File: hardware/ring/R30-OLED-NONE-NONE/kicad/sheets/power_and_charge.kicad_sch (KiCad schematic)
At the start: 19 parts, among them Q1 SI2301 P-FET, Q2 2N7002 gate driver, U3 TP4054, U4 RT9080-33GJ5

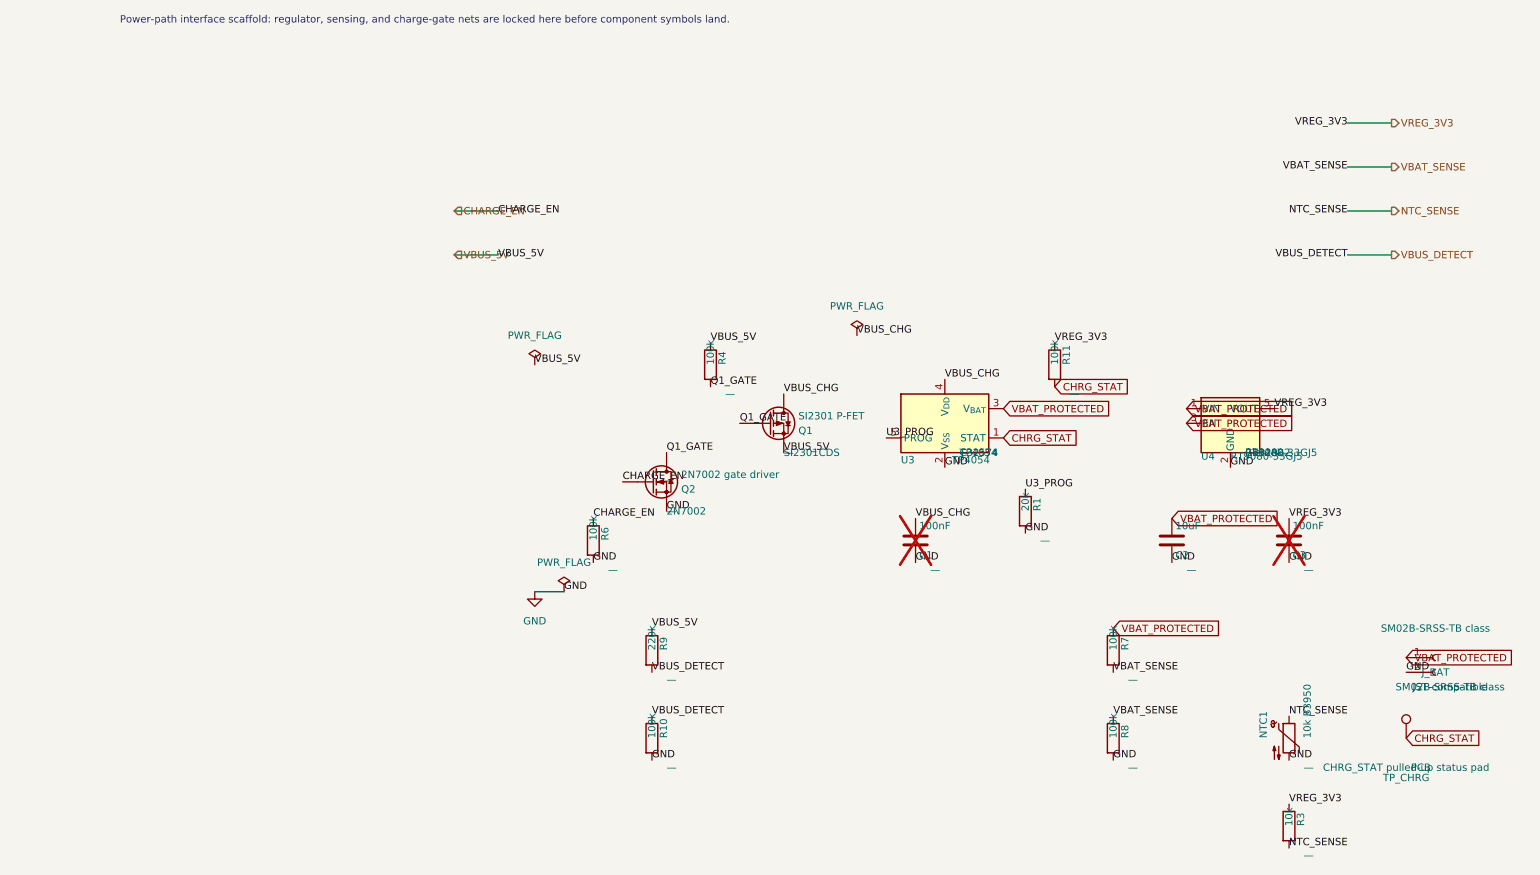
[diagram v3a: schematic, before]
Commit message: fix(r30): reconcile schematic net parity
Sensing mechanism: PAW3204 optical surface tracking.

Form factor and angle: R30 30-degree ring, OLED/NONE/NONE active lane.

Intended use: accessibility-first BLE HID pointing first-board validation.

BOM estimate: active R30 prototype remains about .30-.45, target about .
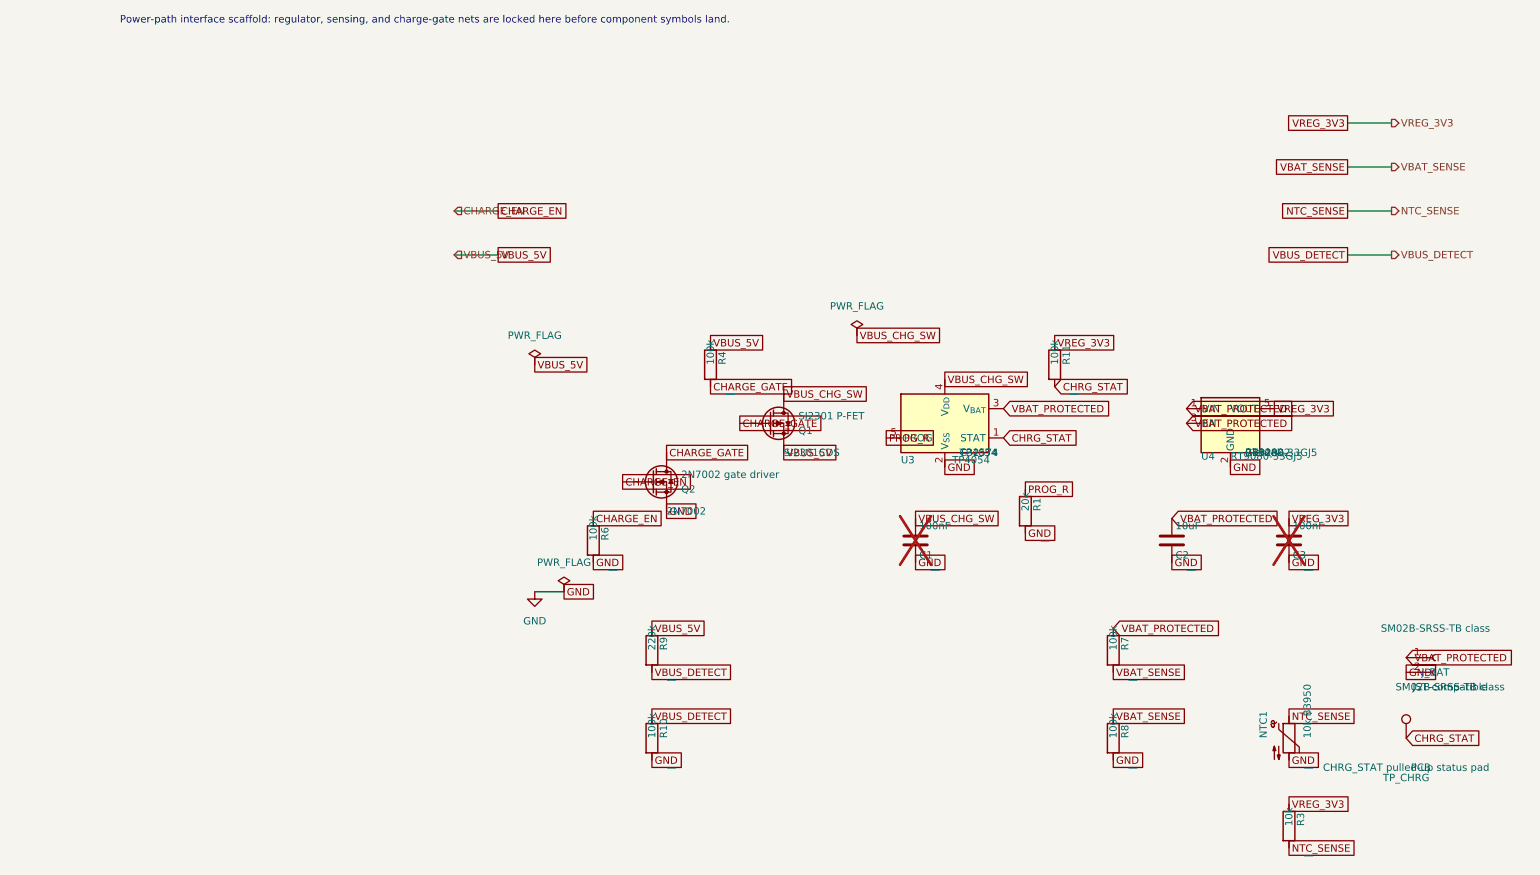
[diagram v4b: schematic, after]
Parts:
- Q1: symbol Device:Q_PMOS -> PowerFinger:SI2301_SOT23_FirstBoard
- Q2: symbol Device:Q_NMOS -> PowerFinger:2N7002_SOT23_FirstBoard
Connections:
- net CHARGE_EN: now also Q2.1 (G); no longer Q2.G
- net GND: now also Q2.2 (S); no longer Q2.S
- net VBUS_5V: now also Q1.3 (S); no longer Q1.S
- removed net Q1_GATE: Q1.G, Q2.D, R4.2
- net U3_PROG renamed PROG_R
- net VBUS_CHG renamed VBUS_CHG_SW
- net VBUS_CHG_SW: now also Q1.2 (D); no longer Q1.D
- new net CHARGE_GATE: Q1.1 (G), Q2.3 (D), R4.2
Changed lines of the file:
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@@
 	(paper "A4")
 	(symbol
-		(lib_id "Device:Q_PMOS")
+		(lib_id "PowerFinger:SI2301_SOT23_FirstBoard")
 		(at 80.01 90.17 0)
 		(unit 1)
@@
 			)
 		)
-		(pin "D"
-		)
-		(pin "G"
-		)
-		(pin "S"
+		(pin "2"
+		)
+		(pin "1"
+		)
+		(pin "3"
 		)
 		(instances
@@
 	)
 	(symbol
-		(lib_id "Device:Q_NMOS")
+		(lib_id "PowerFinger:2N7002_SOT23_FirstBoard")
 		(at 59.69 100.33 0)
 		(unit 1)
@@
 			)
 		)
-		(pin "D"
-		)
-		(pin "G"
-		)
-		(pin "S"
+		(pin "3"
+		)
+		(pin "1"
+		)
+		(pin "2"
 		)
 		(instances
@@
 		)
 	)
-	(label "VBUS_5V"
+	(global_label "VBUS_5V"
+		(shape passive)
 		(at 82.55 95.25 0.0000)
 		(effects
@@
 		)
 	)
-	(label "VBUS_CHG"
+	(global_label "VBUS_CHG_SW"
+		(shape passive)
 		(at 82.55 85.09 0.0000)
 		(effects
@@
 		)
 	)
-	(label "Q1_GATE"
+	(global_label "CHARGE_GATE"
+		(shape passive)
 		(at 74.93 90.17 0.0000)
 		(effects
@@
 		)
 	)
-	(label "Q1_GATE"
+	(global_label "CHARGE_GATE"
+		(shape passive)
 		(at 62.23 95.25 0.0000)
 		(effects
@@
 		)
 	)
-	(label "GND"
+	(global_label "GND"
+		(shape passive)
 		(at 62.23 105.41 0.0000)
 		(effects
@@
 		)
 	)
-	(label "CHARGE_EN"
+	(global_label "CHARGE_EN"
+		(shape passive)
 		(at 54.61 100.33 0.0000)
 		(effects
@@
 		)
 	)
-	(label "VBUS_5V"
+	(global_label "VBUS_5V"
+		(shape passive)
 		(at 69.85 76.2 0.0000)
 		(effects
@@
 		)
 	)
-	(label "Q1_GATE"
+	(global_label "CHARGE_GATE"
+		(shape passive)
 		(at 69.85 83.82 0.0000)
 		(effects
@@
 		)
 	)
-	(label "CHARGE_EN"
+	(global_label "CHARGE_EN"
+		(shape passive)
 		(at 49.53 106.68 0.0000)
 		(effects
@@
 		)
 	)
-	(label "GND"
+	(global_label "GND"
+		(shape passive)
 		(at 49.53 114.3 0.0000)
 		(effects
@@
 		)
 	)
-	(label "GND"
+	(global_label "GND"
+		(shape passive)
 		(at 110.49 97.79 0.0000)
 		(effects
@@
 		)
 	)
-	(label "VBUS_CHG"
+	(global_label "VBUS_CHG_SW"
+		(shape passive)
 		(at 110.49 82.55 0.0000)
 		(effects
@@
 		)
 	)
-	(label "U3_PROG"
+	(global_label "PROG_R"
+		(shape passive)
 		(at 100.33 92.71 0.0000)
 		(effects
@@
 		)
 	)
-	(label "U3_PROG"
+	(global_label "PROG_R"
+		(shape passive)
 		(at 124.46 101.6 0.0000)
 		(effects
@@
 		)
 	)
-	(label "GND"
+	(global_label "GND"
+		(shape passive)
 		(at 124.46 109.22 0.0000)
 		(effects
@@
 		)
 	)
-	(label "VREG_3V3"
+	(global_label "VREG_3V3"
+		(shape passive)
 		(at 129.54 76.2 0.0000)
 		(effects
@@
 		)
 	)
-	(label "GND"
+	(global_label "GND"
+		(shape passive)
 		(at 160.02 97.79 0.0000)
 		(effects
@@
 		)
 	)
-	(label "VREG_3V3"
+	(global_label "VREG_3V3"
+		(shape passive)
 		(at 167.64 87.63 0.0000)
 		(effects
@@
 		)
 	)
-	(label "VBUS_CHG"
+	(global_label "VBUS_CHG_SW"
+		(shape passive)
 		(at 105.41 106.68 0.0000)
 		(effects
@@
 		)
 	)
-	(label "GND"
+	(global_label "GND"
+		(shape passive)
 		(at 105.41 114.3 0.0000)
 		(effects
@@
 		)
 	)
-	(label "GND"
+	(global_label "GND"
+		(shape passive)
 		(at 149.86 114.3 0.0000)
 		(effects
@@
 		)
 	)
-	(label "VREG_3V3"
+	(global_label "VREG_3V3"
+		(shape passive)
 		(at 170.18 106.68 0.0000)
 		(effects
@@
 		)
 	)
-	(label "GND"
+	(global_label "GND"
+		(shape passive)
 		(at 170.18 114.3 0.0000)
 		(effects
@@
 		)
 	)
-	(label "VBAT_SENSE"
+	(global_label "VBAT_SENSE"
+		(shape passive)
 		(at 139.7 133.35 0.0000)
 		(effects
@@
 		)
 	)
-	(label "VBAT_SENSE"
+	(global_label "VBAT_SENSE"
+		(shape passive)
 		(at 139.7 140.97 0.0000)
 		(effects
@@
 		)
 	)
-	(label "GND"
+	(global_label "GND"
+		(shape passive)
 		(at 139.7 148.59 0.0000)
 		(effects
@@
 		)
 	)
-	(label "VBUS_5V"
+	(global_label "VBUS_5V"
+		(shape passive)
 		(at 59.69 125.73 0.0000)
 		(effects
@@
 		)
 	)
-	(label "VBUS_DETECT"
+	(global_label "VBUS_DETECT"
+		(shape passive)
 		(at 59.69 133.35 0.0000)
 		(effects
@@
 		)
 	)
-	(label "VBUS_DETECT"
+	(global_label "VBUS_DETECT"
+		(shape passive)
 		(at 59.69 140.97 0.0000)
 		(effects
@@
 		)
 	)
-	(label "GND"
+	(global_label "GND"
+		(shape passive)
 		(at 59.69 148.59 0.0000)
 		(effects
@@
 		)
 	)
-	(label "VREG_3V3"
+	(global_label "VREG_3V3"
+		(shape passive)
 		(at 170.18 156.21 0.0000)
 		(effects
@@
 		)
 	)
-	(label "NTC_SENSE"
+	(global_label "NTC_SENSE"
+		(shape passive)
 		(at 170.18 163.83 0.0000)
 		(effects
@@
 		)
 	)
-	(label "NTC_SENSE"
+	(global_label "NTC_SENSE"
+		(shape passive)
 		(at 170.18 140.97 0.0000)
 		(effects
@@
 		)
 	)
-	(label "GND"
+	(global_label "GND"
+		(shape passive)
 		(at 170.18 148.59 0.0000)
 		(effects
@@
 		)
 	)
-	(label "VBUS_5V"
+	(global_label "VBUS_5V"
+		(shape passive)
 		(at 39.37 80.01 0)
 		(effects
@@
 		)
 	)
-	(label "VBUS_CHG"
+	(global_label "VBUS_CHG_SW"
+		(shape passive)
 		(at 95.25 74.93 0)
 		(effects
@@
 		)
 	)
-	(label "GND"
+	(global_label "GND"
+		(shape passive)
 		(at 44.45 119.38 0)
 		(effects
@@
 		)
 	)
-	(label "GND"
+	(global_label "GND"
+		(shape passive)
 		(at 190.5 133.35 0)
 		(effects
@@
 		(stroke (width 0) (type default) (color 0 0 0 0))
 	)
-	(label "CHARGE_EN"
+	(global_label "CHARGE_EN"
+		(shape passive)
 		(at 33.02 53.34 0)
 		(effects
@@
 		(stroke (width 0) (type default) (color 0 0 0 0))
 	)
-	(label "VBUS_5V"
+	(global_label "VBUS_5V"
+		(shape passive)
 		(at 33.02 60.96 0)
 		(effects
@@
 		(stroke (width 0) (type default) (color 0 0 0 0))
 	)
-	(label "VREG_3V3"
+	(global_label "VREG_3V3"
+		(shape passive)
 		(at 180.34 38.1 180)
 		(effects
@@
 		(stroke (width 0) (type default) (color 0 0 0 0))
 	)
-	(label "VBAT_SENSE"
+	(global_label "VBAT_SENSE"
+		(shape passive)
 		(at 180.34 45.72 180)
 		(effects
@@
 		(stroke (width 0) (type default) (color 0 0 0 0))
 	)
-	(label "NTC_SENSE"
+	(global_label "NTC_SENSE"
+		(shape passive)
 		(at 180.34 53.34 180)
 		(effects
@@
 		(stroke (width 0) (type default) (color 0 0 0 0))
 	)
-	(label "VBUS_DETECT"
+	(global_label "VBUS_DETECT"
+		(shape passive)
 		(at 180.34 60.96 180)
 		(effects
